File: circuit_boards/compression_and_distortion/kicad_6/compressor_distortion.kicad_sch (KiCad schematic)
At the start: 21 parts, among them J1 dry_in, J2 vcf_board_send_receive, J3 final_out, J4 power_entry, SW1 bypass_switch_A, SW2 bypass_switch_B

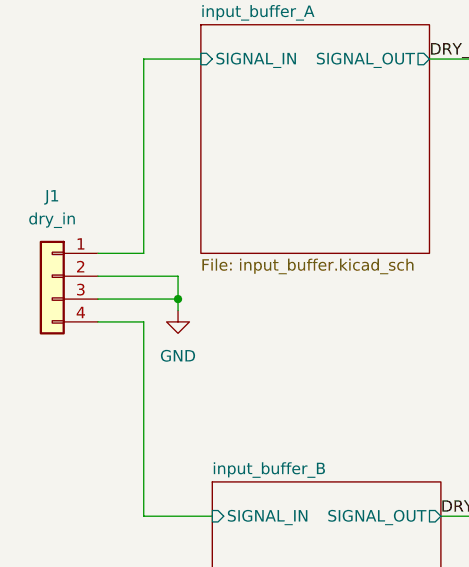
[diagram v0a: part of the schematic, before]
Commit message: Fix a/b swap error and dim LED error
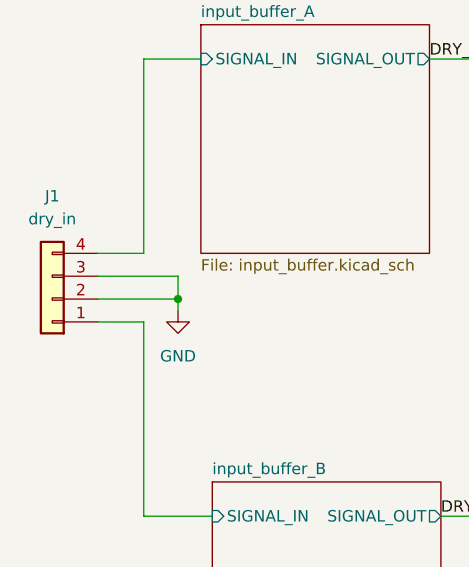
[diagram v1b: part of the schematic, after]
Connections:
- net input_buffer_A/SIGNAL_IN: now also J1.4 (Pin_4); no longer J1.1 (Pin_1)
- net input_buffer_B/SIGNAL_IN: now also J1.1 (Pin_1); no longer J1.4 (Pin_4)
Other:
- moved on the sheet: J1
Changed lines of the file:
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@@
   (title_block
     (title "M.S.M. Stereo Lowpass Filter Pedal")
-    (date "2022-05-26")
-    (rev "0")
+    (date "2023-04-15")
+    (rev "0.1")
     (comment 2 "creativecommons.org/licenses/by/4.0")
     (comment 3 "License: CC by 4.0")
@@
     (pin "6")
   )
-  (symbol (lib_id "Connector_Generic:Conn_01x04") (at 20.32 59.69 0) (mirror y) (unit 1)
+  (symbol (lib_id "Connector_Generic:Conn_01x04") (at 20.32 62.23 180) (unit 1)
     (in_bom yes) (on_board yes) (fields_autoplaced)
     (property "Reference" "J1" (id 0) (at 20.32 50.8 0))
     (property "Value" "dry_in" (id 1) (at 20.32 53.34 0))
-    (property "Footprint" "Connector_Molex:Molex_KK-254_AE-6410-04A_1x04_P2.54mm_Vertical" (id 2) (at 20.32 59.69 0)
-      (effects (font (size 1.27 1.27)) hide)
-    )
-    (property "Datasheet" "~" (id 3) (at 20.32 59.69 0)
+    (property "Footprint" "Connector_Molex:Molex_KK-254_AE-6410-04A_1x04_P2.54mm_Vertical" (id 2) (at 20.32 62.23 0)
+      (effects (font (size 1.27 1.27)) hide)
+    )
+    (property "Datasheet" "~" (id 3) (at 20.32 62.23 0)
       (effects (font (size 1.27 1.27)) hide)
     )
@@
     )
     (path "/8a27587f-d1cd-4e5e-8c37-1c9be5f06308/84605a75-e941-4ac7-ae98-08f69b5b13cb"
-      (reference "R44") (unit 1) (value "3k3") (footprint "Resistor_SMD:R_0805_2012Metric")
+      (reference "R44") (unit 1) (value "100") (footprint "Resistor_SMD:R_0805_2012Metric")
     )
     (path "/8a27587f-d1cd-4e5e-8c37-1c9be5f06308/1ba93d4d-7c8f-4935-9cd9-b543f503dc19"
-      (reference "R45") (unit 1) (value "3k3") (footprint "Resistor_SMD:R_0805_2012Metric")
+      (reference "R45") (unit 1) (value "100") (footprint "Resistor_SMD:R_0805_2012Metric")
     )
     (path "/7f86df69-acb0-4c00-b743-ed1f86528b3b/41961c06-24a8-4569-a7c3-7889fc212ff6"
